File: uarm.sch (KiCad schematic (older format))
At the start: 15 parts, among them P1 CONN_01X02, U1 LM2596_Buck_Board, U2 MicroView, U3 esp-01, U4 LM2596_Buck_Board

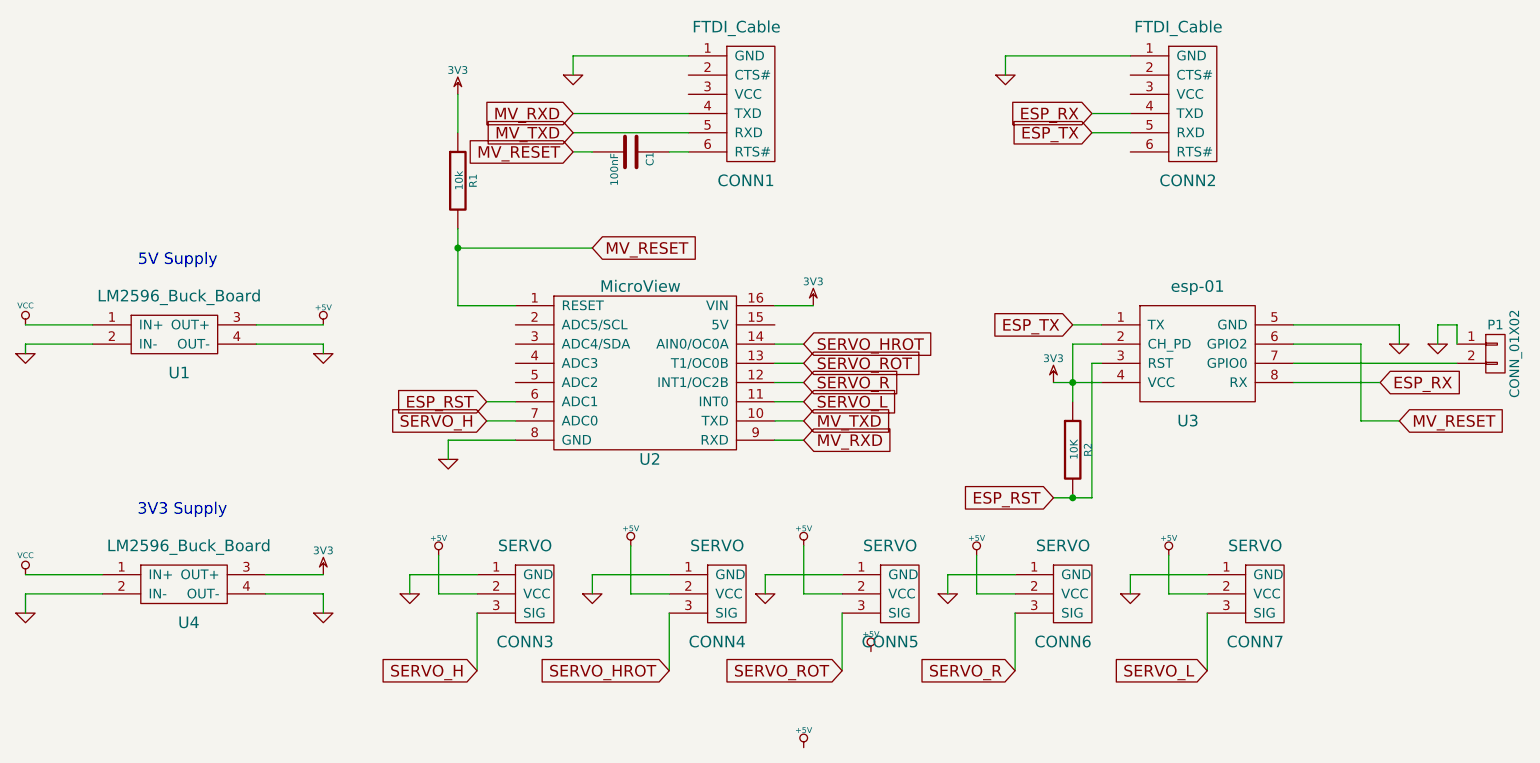
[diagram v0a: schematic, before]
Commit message: first working prototype created
dropped mutal reset pin handling from esp and microview; now esets
have to occur in software or via a hard power down/up

rotated LM2569 boards to simplify routing

this design has been milled and soldered and works perfectly for
programming both the microview and esp-01 with a FTDI ft232r 3v3
cable.
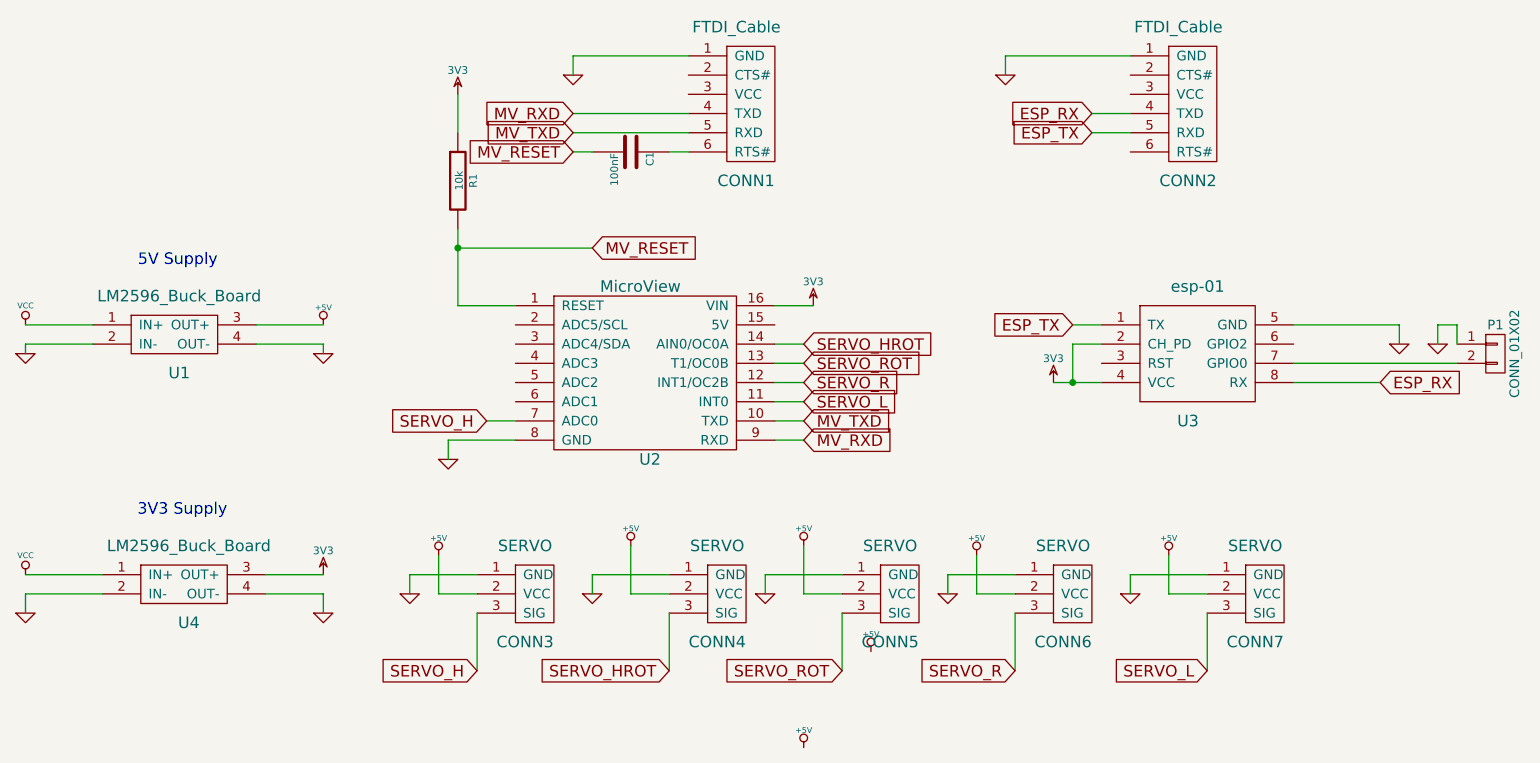
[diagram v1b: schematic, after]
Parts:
- removed R2: 10K, Discret:R1, symbol R
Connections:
- net MV_RESET: no longer U3.6 (GPIO2)
- net ESP_RST: no longer names the net of U3.3 (RST)
- net ESP_RST: no longer U2.6 (ADC1)
